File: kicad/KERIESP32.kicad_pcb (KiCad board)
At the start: 2 copper layers, 72 x 96 mm, 60 parts, among them P1 GPIO_0-19, P2 GPIO_21-27, P3 GPIO_32-39, P4 SD_DETECT, P5 USB_Micro_B, P6 GND, P7 Power, SW1 IO0, SW2 RST, U1 ESP-WROOM-32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

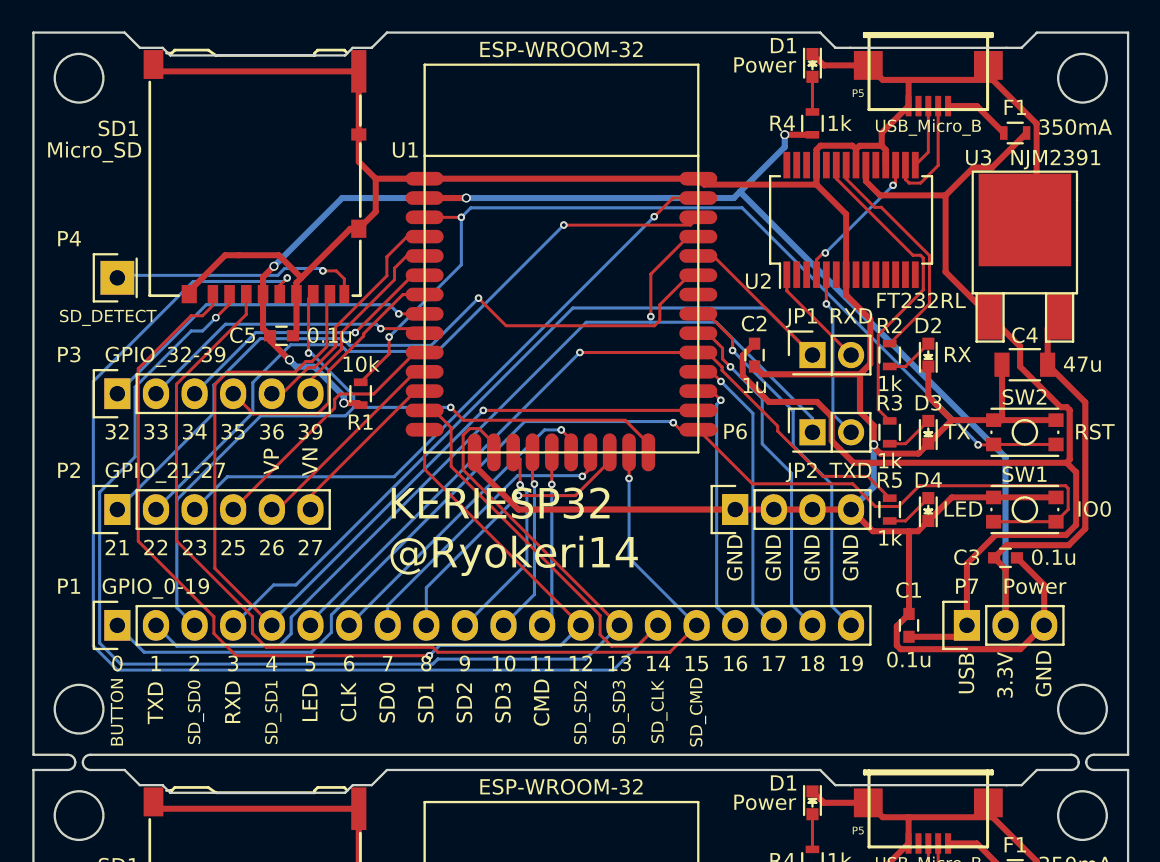
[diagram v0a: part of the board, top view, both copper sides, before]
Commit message: 部品表，回路図PDFを生成
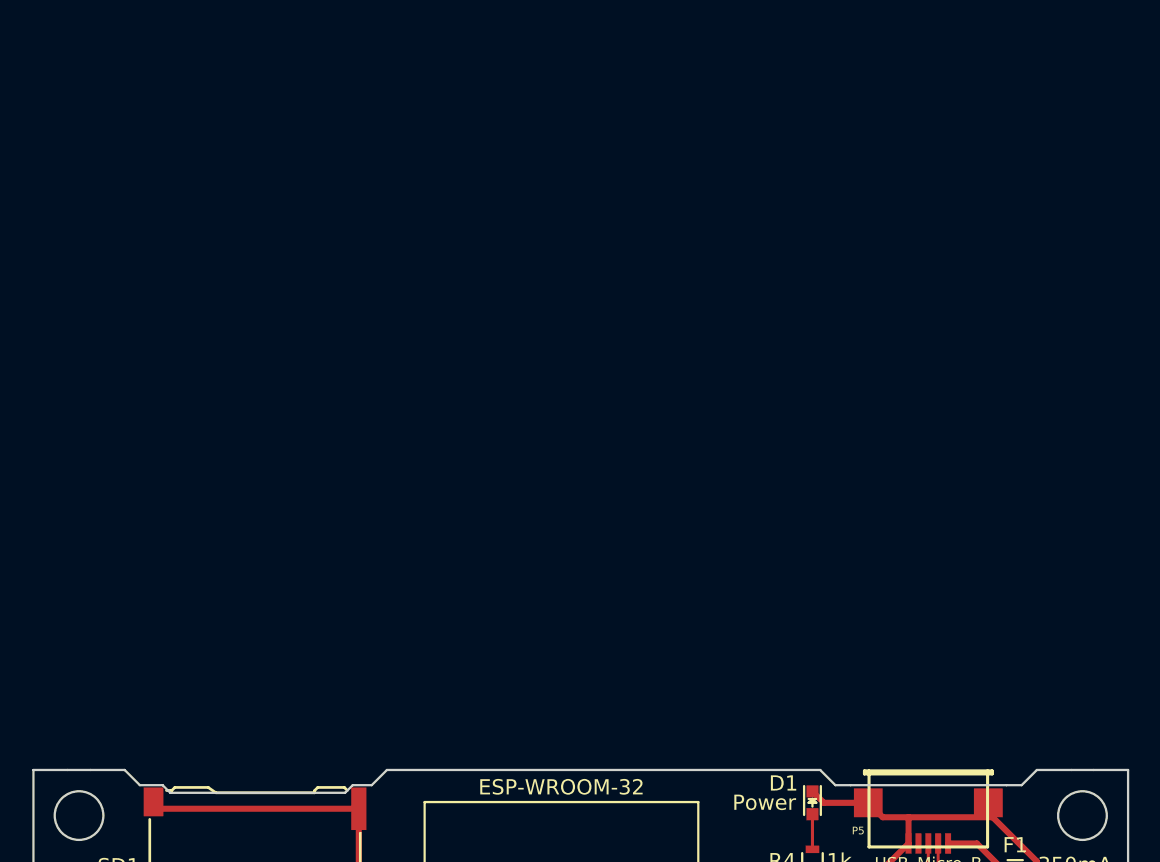
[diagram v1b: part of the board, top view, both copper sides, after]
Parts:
- removed the C1 at (179.1, 70.9)
- removed the C2 at (168.9, 53.1)
- removed the C3 at (185.4, 66.4)
- removed the C4 at (186.7, 53.7)
- removed the C5 at (137.8, 51.8)
- removed the D1 at (172.7, 34.0)
- removed the D2 at (180.3, 53.1)
- removed the D3 at (180.3, 58.2)
- removed the D4 at (180.3, 63.3)
- removed the F1 at (186.1, 38.5)
- removed the JP1 at (172.7, 53.1)
- removed the JP2 at (172.7, 58.2)
- removed the P1 at (127.0, 70.9)
- removed the P2 at (127.0, 63.3)
- removed the P3 at (127.0, 55.6)
- removed the P4 at (127.0, 48.0)
- removed the P5 at (180.3, 34.0)
- removed the P6 at (167.6, 63.3)
- removed the P7 at (182.9, 70.9)
- removed the R1 at (143.0, 55.6)
- removed the R2 at (177.8, 53.1)
- removed the R3 at (177.8, 58.2)
- removed the R4 at (172.7, 37.9)
- removed the R5 at (177.8, 63.3)
- removed the SD1 at (136.5, 31.6)
- removed the SW1 at (186.7, 63.3)
- removed the SW2 at (186.7, 58.2)
- removed the U1 at (156.2, 46.8)
- removed the U2 at (175.3, 44.2)
- removed the U3 at (186.7, 50.6)
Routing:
- net GND: track 457.3 -> 228.6 mm, vias 2 -> 1
- net +3V3: track 236.3 -> 118.2 mm, vias 10 -> 5
- net SDIO_CLK: track 195.7 -> 97.8 mm, vias 2 -> 1
- net SDIO_SD3: track 166.0 -> 83.0 mm, vias 2 -> 1
- net +5V: track 165.6 -> 82.8 mm
- net BUTTON: track 159.6 -> 79.8 mm, vias 2 -> 1
- net SDIO_CMD: track 139.9 -> 70.0 mm, vias 2 -> 1
- net SDIO_SD2: track 139.1 -> 69.5 mm, vias 2 -> 1
- net UART_TX: track 128.1 -> 64.0 mm, vias 2 -> 1
- net SDIO_SD1: track 126.7 -> 63.4 mm, vias 2 -> 1
- net ENABLE: track 123.8 -> 61.9 mm, vias 6 -> 3
- net UART_RX: track 116.5 -> 58.2 mm
- net SDIO_SD0: track 105.5 -> 52.8 mm, vias 4 -> 2
- net LED: track 99.9 -> 50.0 mm, vias 2 -> 1
- net Net-(P2-Pad1): track 96.3 -> 48.1 mm, vias 2 -> 1
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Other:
- board size 72 x 96 mm -> 72 x 47.5 mm

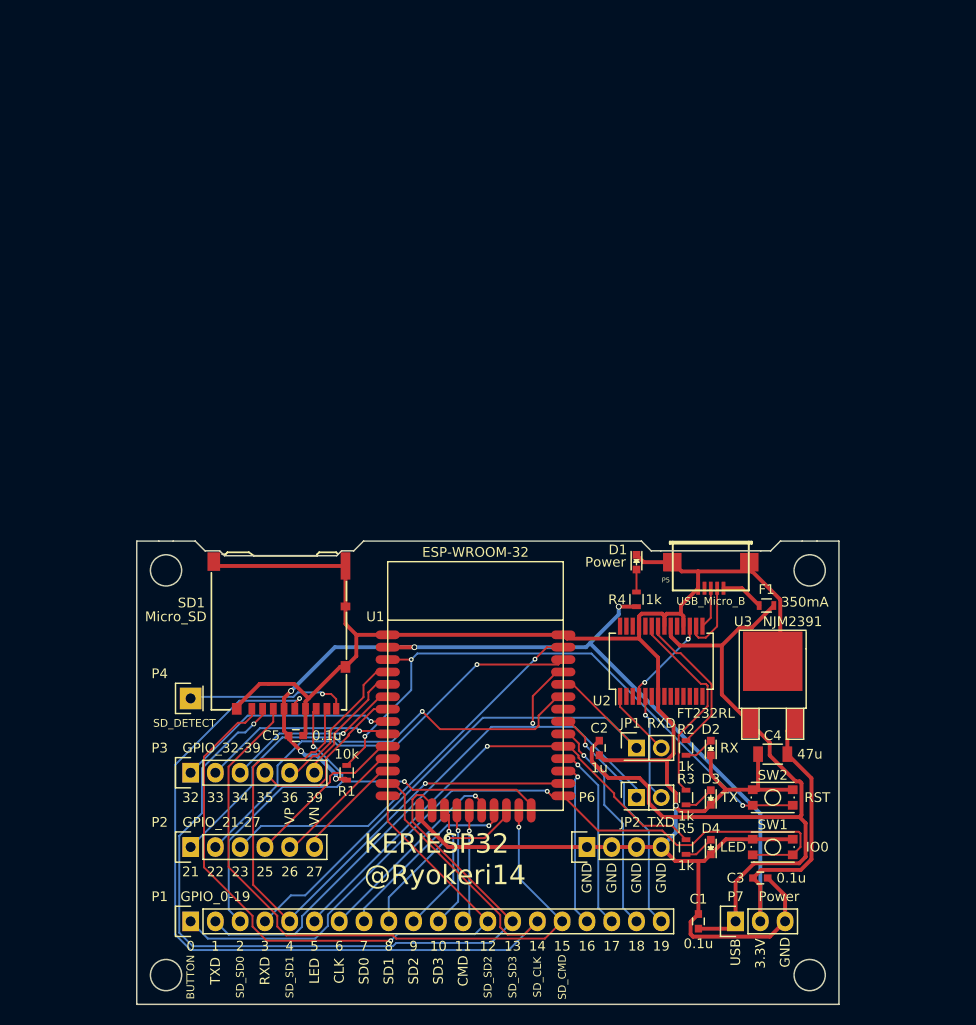
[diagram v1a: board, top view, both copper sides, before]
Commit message: 台形型変換基板を設計
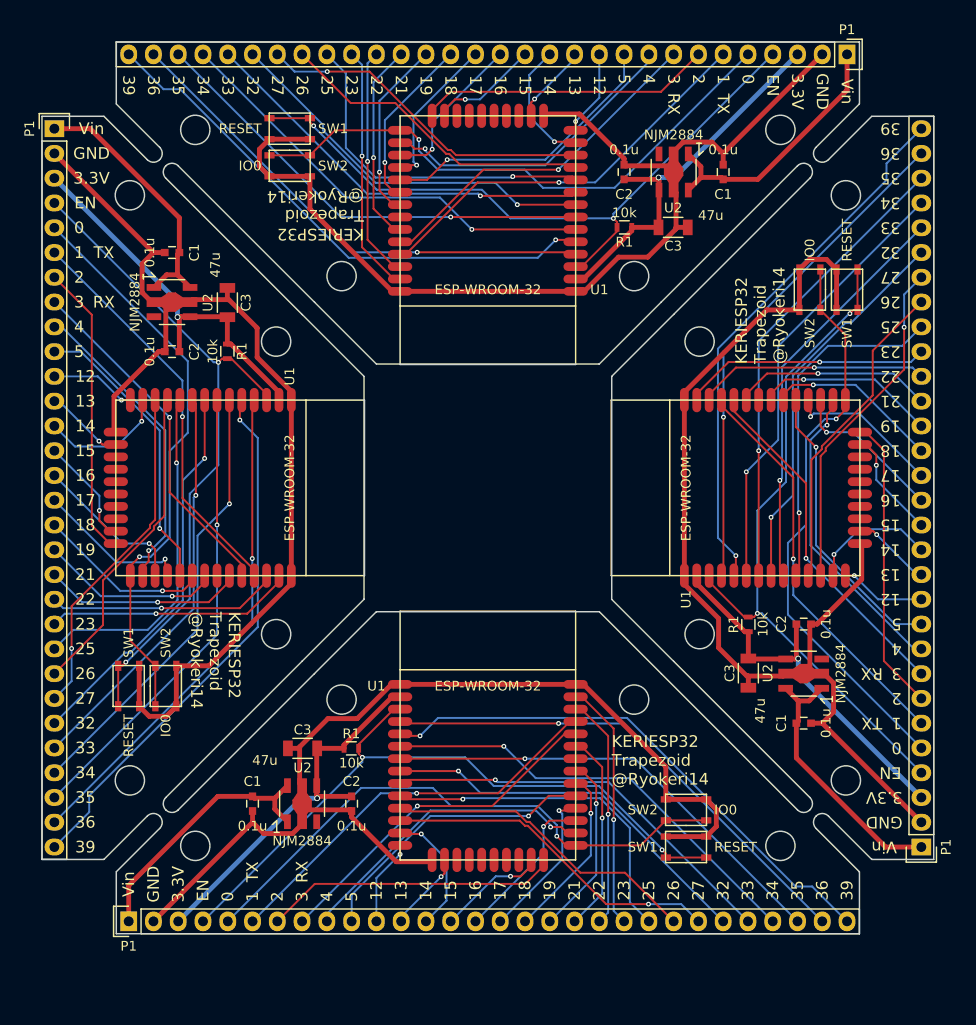
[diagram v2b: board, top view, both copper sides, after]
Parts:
- removed the C1 at (179.1, 119.4)
- removed the C2 at (168.9, 101.6)
- removed the C3 at (185.4, 114.9)
- removed C4: 47u, Capacitors_SMD:C_1206
- removed C5: 0.1u, Capacitors_SMD:C_0603
- removed D1: Power, LEDs:LED_0603
- removed D2: RX, LEDs:LED_0603
- removed D3: TX, LEDs:LED_0603
- removed D4: LED, LEDs:LED_0603
- removed F1: 350mA, Resistors_SMD:R_0603
- removed JP1: RXD, Pin_Headers:Pin_Header_Straight_2x01
- removed JP2: TXD, Pin_Headers:Pin_Header_Straight_2x01
- removed the P1 at (127.0, 119.4)
- removed P2: GPIO_21-27, Socket_Strips:Socket_Strip_Straight_1x06
- removed P3: GPIO_32-39, Socket_Strips:Socket_Strip_Straight_1x06
- removed P4: SD_DETECT, Socket_Strips:Socket_Strip_Straight_1x01
- removed P5: USB_Micro_B, kerikun11:USB_Micro_B_smd
- removed P6: GND, Socket_Strips:Socket_Strip_Straight_1x04
- removed P7: Power, Socket_Strips:Socket_Strip_Straight_1x03
- removed the R1 at (143.0, 104.1)
- removed R2, R3, R4, R5: 1k, Resistors_SMD:R_0603
- removed SD1: Micro_SD, conn-io:HIROSE-MICROSD-DM3AT-SF
- removed the SW1 at (186.7, 111.8)
- removed the SW2 at (186.7, 106.7)
- removed the U1 at (156.2, 95.2)
- removed the U2 at (175.3, 92.7)
- removed U3: NJM2391, TO_SOT_Packages_SMD:TO-252-2Lead
- added C1: 0.1u, Capacitors_SMD:C_0603, F.Cu at (181.6, 42.5)
- added C1: 0.1u, Capacitors_SMD:C_0603, F.Cu at (125.1, 50.8)
- added C1: 0.1u, Capacitors_SMD:C_0603, F.Cu at (189.9, 99.1)
- added C1: 0.1u, Capacitors_SMD:C_0603, F.Cu at (133.3, 107.3)
- added C2: 0.1u, Capacitors_SMD:C_0603, F.Cu at (171.4, 42.5)
- added C2: 0.1u, Capacitors_SMD:C_0603, F.Cu at (125.1, 61.0)
- added C2: 0.1u, Capacitors_SMD:C_0603, F.Cu at (189.9, 88.9)
- added C2: 0.1u, Capacitors_SMD:C_0603, F.Cu at (143.5, 107.3)
- added C3: 47u, Capacitors_SMD:C_1206, F.Cu at (176.5, 48.2)
- added C3: 47u, Capacitors_SMD:C_1206, F.Cu at (130.8, 55.9)
- added C3: 47u, Capacitors_SMD:C_1206, F.Cu at (184.2, 93.9)
- added C3: 47u, Capacitors_SMD:C_1206, F.Cu at (138.5, 101.6)
- added P1: CONN_01X30, Pin_Headers:Pin_Header_Straight_1x30, F.Cu at (194.3, 30.5)
- added P1: CONN_01X30, Pin_Headers:Pin_Header_Straight_1x30, F.Cu at (113.0, 38.1)
- added P1: CONN_01X30, Pin_Headers:Pin_Header_Straight_1x30, F.Cu at (201.9, 111.8)
- added P1: CONN_01X30, Pin_Headers:Pin_Header_Straight_1x30, F.Cu at (120.7, 119.4)
- added R1: 10k, Resistors_SMD:R_0603, F.Cu at (171.5, 48.2)
- added R1: 10k, Resistors_SMD:R_0603, F.Cu at (130.8, 60.9)
- added R1: 10k, Resistors_SMD:R_0603, F.Cu at (184.2, 88.9)
- added R1: 10k, Resistors_SMD:R_0603, F.Cu at (143.5, 101.6)
- added SW1: RESET, kerikun11:SW_PUSH, F.Cu at (137.2, 38.1)
- added SW1: RESET, kerikun11:SW_PUSH, F.Cu at (120.7, 95.2)
- added SW1: RESET, kerikun11:SW_PUSH, F.Cu at (194.3, 54.6)
- added SW1: RESET, kerikun11:SW_PUSH, F.Cu at (177.8, 111.8)
- added SW2: IO0, kerikun11:SW_PUSH, F.Cu at (137.2, 41.9)
- added SW2: IO0, kerikun11:SW_PUSH, F.Cu at (124.5, 95.2)
- added SW2: IO0, kerikun11:SW_PUSH, F.Cu at (190.5, 54.6)
- added SW2: IO0, kerikun11:SW_PUSH, F.Cu at (177.8, 108.0)
- added U1: ESP-WROOM-32, kerikun11:ESP-WROOM-32, F.Cu at (157.5, 49.5)
- added U1: ESP-WROOM-32, kerikun11:ESP-WROOM-32, F.Cu at (132.1, 74.9)
- added U1: ESP-WROOM-32, kerikun11:ESP-WROOM-32, F.Cu at (182.9, 74.9)
- added U1: ESP-WROOM-32, kerikun11:ESP-WROOM-32, F.Cu at (157.5, 100.3)
- added U2: NJM2884, TO_SOT_Packages_SMD:SOT89-5_Housing, F.Cu at (176.5, 42.5)
- added U2: NJM2884, TO_SOT_Packages_SMD:SOT89-5_Housing, F.Cu at (125.1, 55.9)
- added U2: NJM2884, TO_SOT_Packages_SMD:SOT89-5_Housing, F.Cu at (189.9, 94.0)
- added U2: NJM2884, TO_SOT_Packages_SMD:SOT89-5_Housing, F.Cu at (138.4, 107.3)
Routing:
- net IO0: track 0.00 -> 235.6 mm, vias 0 -> 4
- net Net-(P1-Pad30): track 0.00 -> 221.3 mm, vias 0 -> 4
- net ENABLE: track 61.9 -> 282.5 mm, vias 3 -> 8
- net Net-(P1-Pad29): track 0.00 -> 207.1 mm, vias 0 -> 4
- net GND: track 228.6 -> 426.8 mm, vias 1 -> 0
- net Net-(P1-Pad28): track 0.00 -> 190.6 mm, vias 0 -> 4
- net Net-(P1-Pad27): track 0.00 -> 182.6 mm, vias 0 -> 4
- net Net-(P1-Pad26): track 0.00 -> 167.3 mm, vias 0 -> 4
- net Net-(P1-Pad6): track 0.00 -> 166.5 mm, vias 0 -> 4
- net Net-(P1-Pad25): track 0.00 -> 159.4 mm, vias 0 -> 4
- net Net-(P1-Pad22): track 0.00 -> 141.6 mm, vias 0 -> 4
- net Net-(P1-Pad24): track 0.00 -> 139.5 mm, vias 0 -> 4
- net Net-(P1-Pad23): track 0.00 -> 131.4 mm
- net Net-(P1-Pad8): track 19.5 -> 144.0 mm, vias 1 -> 4
- net Net-(P1-Pad9): track 18.6 -> 126.9 mm, vias 1 -> 4
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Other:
- board size 72 x 47.5 mm -> 91.4 x 91.4 mm
- net class Power: trace_width 0.4 -> 0.5
- board text added: "EN"
- board text added: "KERIESP32 Trapezoid @Ryokeri14"
- board text added: "RX"
- board text added: "TX"
- board text added: "Vin"
- board text removed: "10"
- board text removed: "11"
- board text removed: "6"
- board text removed: "7"
- board text removed: "8"
- board text removed: "9"
- board text removed: "BUTTON"
- board text removed: "CLK"
- board text removed: "CMD"
- board text removed: "KERIESP32 @Ryokeri14"
- board text removed: "LED"
- board text removed: "RXD"
- board text removed: "SD0"
- board text removed: "SD1"
- board text removed: "SD2"
- board text removed: "SD3"
- board text removed: "SD_CLK"
- board text removed: "SD_CMD"
- board text removed: "SD_SD0"
- board text removed: "SD_SD1"
- board text removed: "SD_SD2"
- board text removed: "SD_SD3"
- board text removed: "TXD"
- board text removed: "USB"
- board text removed: "VN"
- board text removed: "VP"

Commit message: 台形基板にSDカードを設置
裏面にMicroSDスロットを取り付け．
形は変わらず
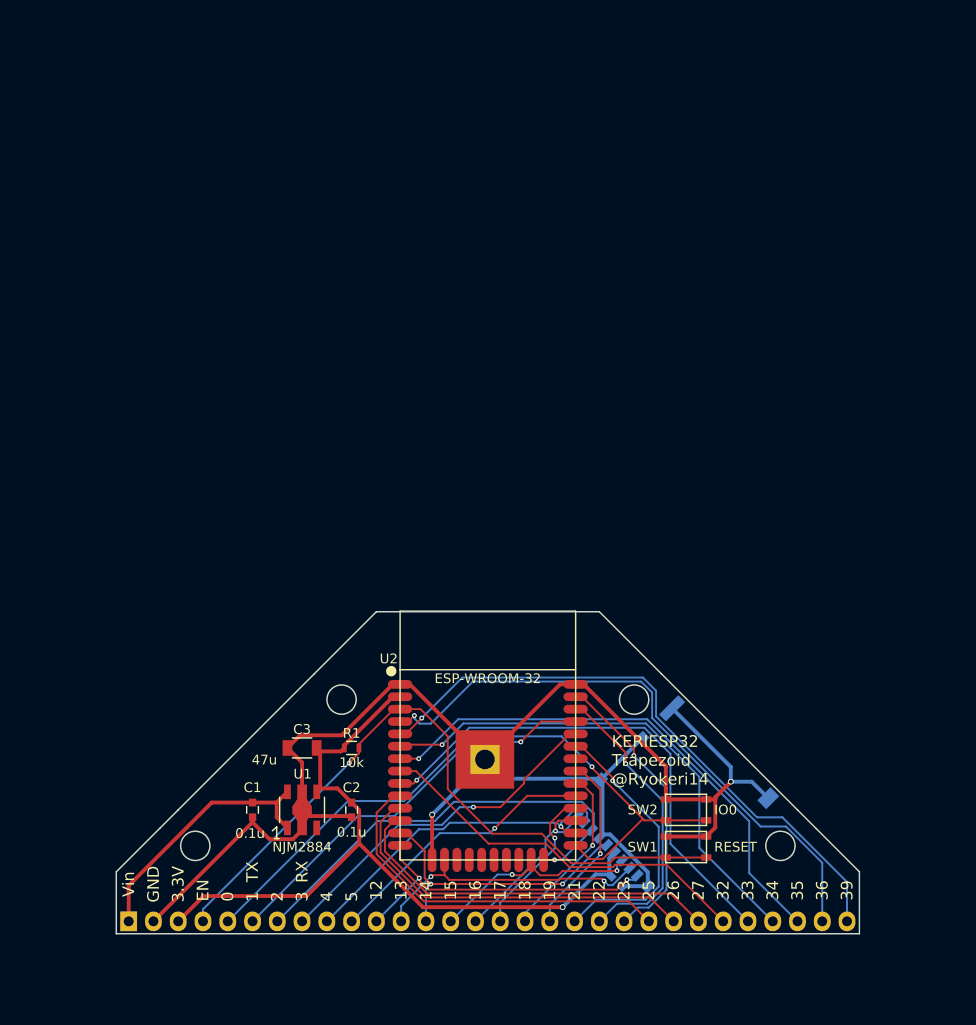
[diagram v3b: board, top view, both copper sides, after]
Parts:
- removed the C1 at (181.6, 42.5)
- removed the C1 at (125.1, 50.8)
- removed the C1 at (189.9, 99.1)
- removed the C2 at (171.4, 42.5)
- removed the C2 at (125.1, 61.0)
- removed the C2 at (189.9, 88.9)
- removed the C3 at (176.5, 48.2)
- removed the C3 at (130.8, 55.9)
- removed the C3 at (184.2, 93.9)
- removed the P1 at (194.3, 30.5)
- removed the P1 at (113.0, 38.1)
- removed the P1 at (201.9, 111.8)
- removed the R1 at (171.5, 48.2)
- removed the R1 at (130.8, 60.9)
- removed the R1 at (184.2, 88.9)
- removed the SW1 at (137.2, 38.1)
- removed the SW1 at (120.7, 95.2)
- removed the SW1 at (194.3, 54.6)
- removed the SW2 at (137.2, 41.9)
- removed the SW2 at (124.5, 95.2)
- removed the SW2 at (190.5, 54.6)
- removed the U1 at (157.5, 49.5)
- removed the U1 at (132.1, 74.9)
- removed the U1 at (182.9, 74.9)
- removed the U1 at (157.5, 100.3)
- removed the U2 at (176.5, 42.5)
- removed the U2 at (125.1, 55.9)
- removed the U2 at (189.9, 94.0)
- added C4: 0.1u, Capacitors_SMD:C_0603, B.Cu at (170.7, 115.3)
- added SD1: Micro_SD, kerikun11:HIROSE-MICROSD-DM3AT-SF, B.Cu at (182.9, 100.1)
- added U2: ESP-WROOM-32, kerikun11:ESP-WROOM-32, F.Cu at (157.5, 100.3)
- P1: moved to B.Cu
- moved C1 0.64 mm to (133.3, 108.0)
- moved C2 0.64 mm to (143.5, 108.0)
- moved U1 0.64 mm to (138.4, 108.0)
- moved C3 0.06 mm to (138.4, 101.6)
- moved R1 0.05 mm to (143.5, 101.6)
- turned P1 to 270 degrees
- renumbered U2 to U1
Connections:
- P1 pad 11: Net-(P1-Pad11) -> SD_SD2
- P1 pad 12: Net-(P1-Pad12) -> SD_SD3
- P1 pad 13: Net-(P1-Pad13) -> SD_CLK
- P1 pad 14: Net-(P1-Pad14) -> SD_CMD
- P1 pad 15: Net-(P1-Pad15) -> SD_DETECT
- P1 pad 7: Net-(P1-Pad7) -> SD_SD0
- P1 pad 9: Net-(P1-Pad9) -> SD_SD1
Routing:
- net GND: track 426.8 -> 168.5 mm, vias 0 -> 2
- net ENABLE: track 282.5 -> 71.9 mm, vias 8 -> 1
- net IO0: track 235.6 -> 69.8 mm, vias 4 -> 1
- net Net-(P1-Pad30): track 221.3 -> 62.5 mm, vias 4 -> 1
- net Net-(P1-Pad29): track 207.1 -> 61.1 mm, vias 4 -> 1
- net Net-(P1-Pad28): track 190.6 -> 54.1 mm, vias 4 -> 1
- net Net-(P1-Pad27): track 182.6 -> 51.9 mm, vias 4 -> 1
- net Net-(P1-Pad9): track 126.9 -> 0.00 mm, vias 4 -> 0
- net Net-(P1-Pad6): track 166.5 -> 41.6 mm, vias 4 -> 1
- net Net-(P1-Pad7): track 121.1 -> 0.00 mm
- net Net-(P1-Pad25): track 159.4 -> 39.7 mm, vias 4 -> 0
- net Net-(P1-Pad26): track 167.3 -> 51.7 mm, vias 4 -> 1
- net Net-(P1-Pad8): track 144.0 -> 36.2 mm, vias 4 -> 1
- net Net-(P1-Pad22): track 141.6 -> 38.1 mm, vias 4 -> 0
- net Net-(P1-Pad24): track 139.5 -> 39.3 mm, vias 4 -> 0
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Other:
- board size 91.4 x 91.4 mm -> 76.2 x 33 mm
- net class Power: trace_width 0.5 -> 0.4
